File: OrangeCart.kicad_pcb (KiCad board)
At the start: 4 copper layers, 62 x 50 mm, 131 parts, among them J1 Conn_02x11_Odd_Even, J2 UART, J3 USB_B_Mini, J4 MicroSd, J6 JTAG, SW1 SW_Push, U1 FAN53541, U10 NCP115-2.5, U11 74AHCV17A, U12 74LVC3G17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

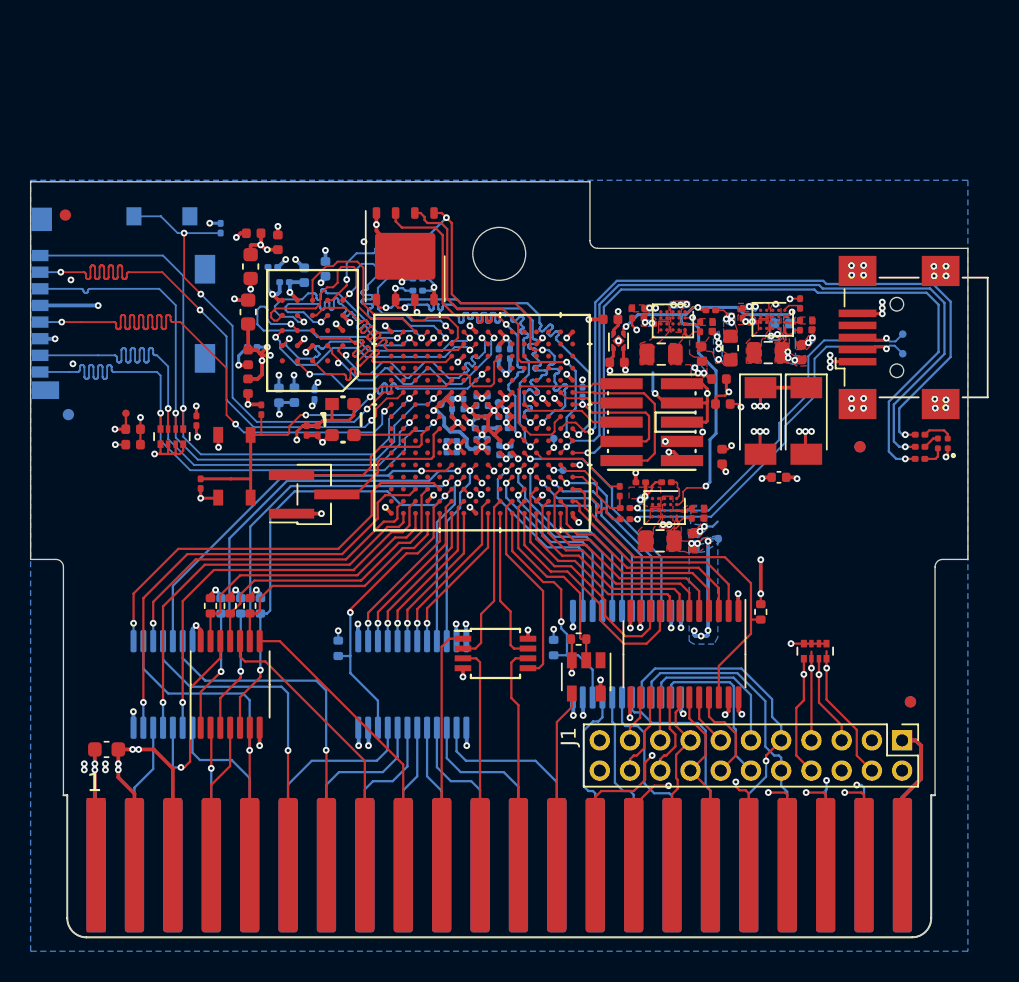
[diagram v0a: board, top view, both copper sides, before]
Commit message: Replace LED with THT version
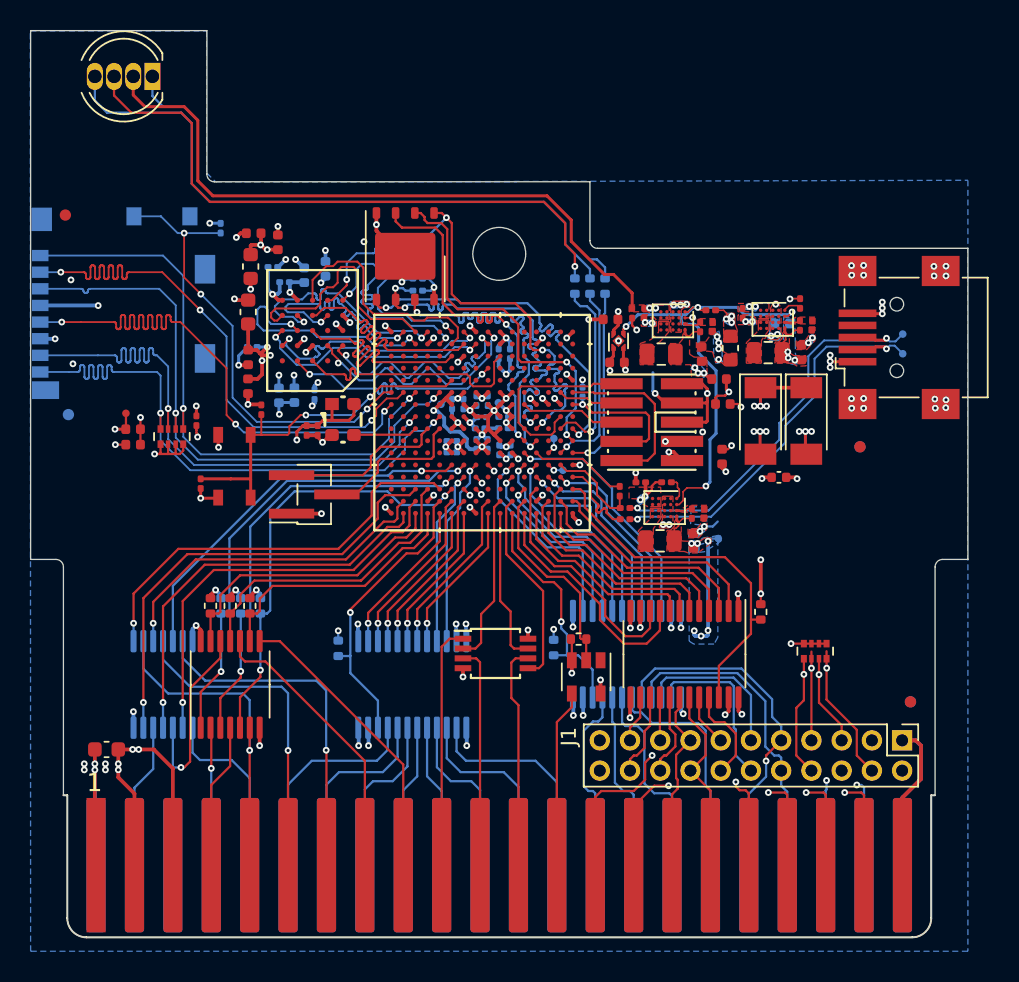
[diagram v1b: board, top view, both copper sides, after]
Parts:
- D1: value LED_ARGB -> LED_RABG; footprint gkl_led:0404LED_RGB -> LED_THT:LED_D5.0mm-4_RGB
- R22: value 1.5k -> 249; footprint Resistor_SMD:R_0201_0603Metric -> Resistor_SMD:R_0402_1005Metric; moved to B.Cu
- R23: value 4.7k -> 120; footprint Resistor_SMD:R_0201_0603Metric -> Resistor_SMD:R_0402_1005Metric; moved to B.Cu
- R24: value 3.57k -> 120; footprint Resistor_SMD:R_0201_0603Metric -> Resistor_SMD:R_0402_1005Metric; moved to B.Cu
- moved D1 57.6 mm to (57.1, 73.1), turned to 180 degrees
- moved R24 24.9 mm to (85.0, 87.0), turned to 90 degrees
- moved R23 24.3 mm to (86.0, 87.0), turned to 90 degrees
- moved R22 23.8 mm to (87.0, 87.0), turned to 90 degrees
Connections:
- D1 pad 1: P3.3V -> Net-(D1-Pad1)
- D1 pad 2: Net-(D1-Pad2) -> VSYS
- R22 pad 2: Net-(D1-Pad2) -> Net-(D1-Pad1)
- R23 pad 2: Net-(D1-Pad3) -> Net-(D1-Pad4)
- R24 pad 2: Net-(D1-Pad4) -> Net-(D1-Pad3)
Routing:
- net VSYS: track 33.9 -> 77.7 mm
- net Net-(D1-Pad4): track 2.03 -> 42.7 mm
- net Net-(D1-Pad1): track 0.00 -> 39.8 mm
- net Net-(D1-Pad3): track 1.08 -> 40.9 mm, vias 0 -> 1
- net LED_R: track 47.4 -> 12.2 mm, vias 2 -> 1
- net LED_G: track 47.7 -> 12.7 mm, vias 2 -> 1
- net LED_B: track 46.9 -> 12.5 mm, vias 2 -> 1
- net Net-(D1-Pad2): track 1.47 -> 0.00 mm
- net P3.3V: track 49.0 -> 48.4 mm, vias 26 -> 25
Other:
- board size 62 x 50 mm -> 62 x 60 mm

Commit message: Replace pushbutton with THT version
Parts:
- SW1: footprint gkl_misc:PTS_810_SMT_Switch -> TE:TPB11CGPC004
- moved FID5 23.7 mm to (50.7, 71.8)
- moved SW1 21.1 mm to (52.5, 80.3)
- moved C76 15.5 mm to (61.6, 84.6), turned to 0 degrees
- moved R4 11.7 mm to (61.6, 83.8), turned to 180 degrees
- moved FID4 10.5 mm to (50.7, 71.8)
- moved D1 0.50 mm to (57.1, 73.6)
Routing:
- net USER_BUTTON: track 23.9 -> 33.8 mm
- net GND: track 145.5 -> 143.7 mm, vias 118 -> 117
- net VSYS: track 77.7 -> 77.2 mm
- net Net-(D1-Pad4): track 42.7 -> 42.2 mm
- net Net-(D1-Pad3): track 40.9 -> 40.4 mm
- net Net-(D1-Pad1): track 39.8 -> 39.3 mm

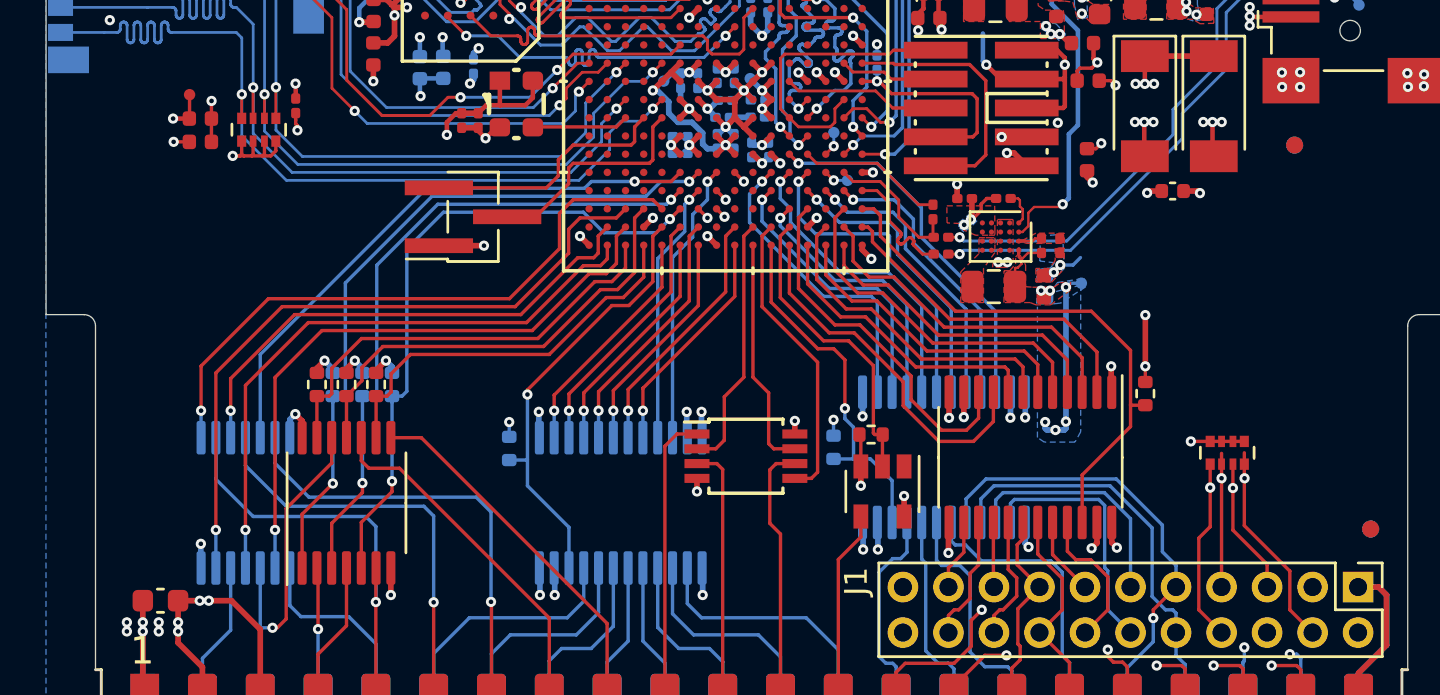
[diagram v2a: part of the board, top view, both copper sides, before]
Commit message: Moved fiducials
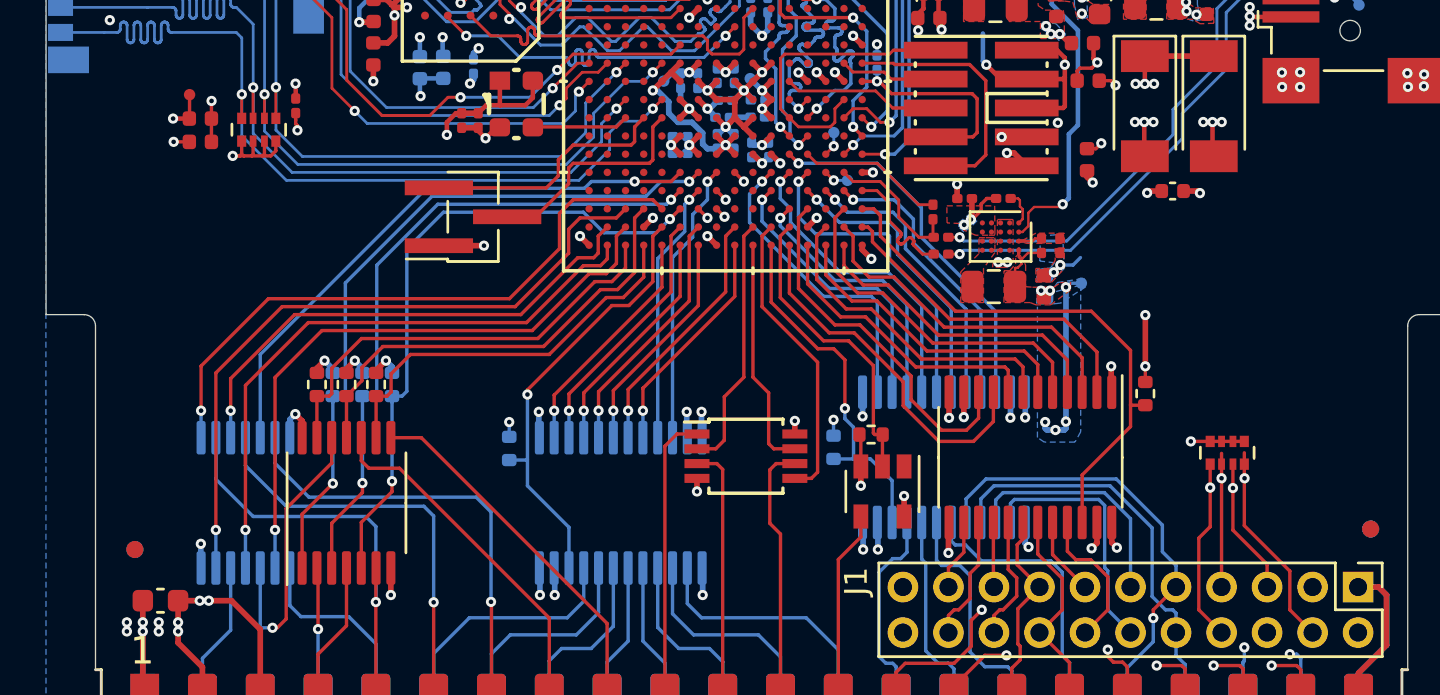
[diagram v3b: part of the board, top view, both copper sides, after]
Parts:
- moved FID3 54.0 mm to (52.9, 115.4)
- moved FID6 54.0 mm to (52.9, 115.4)

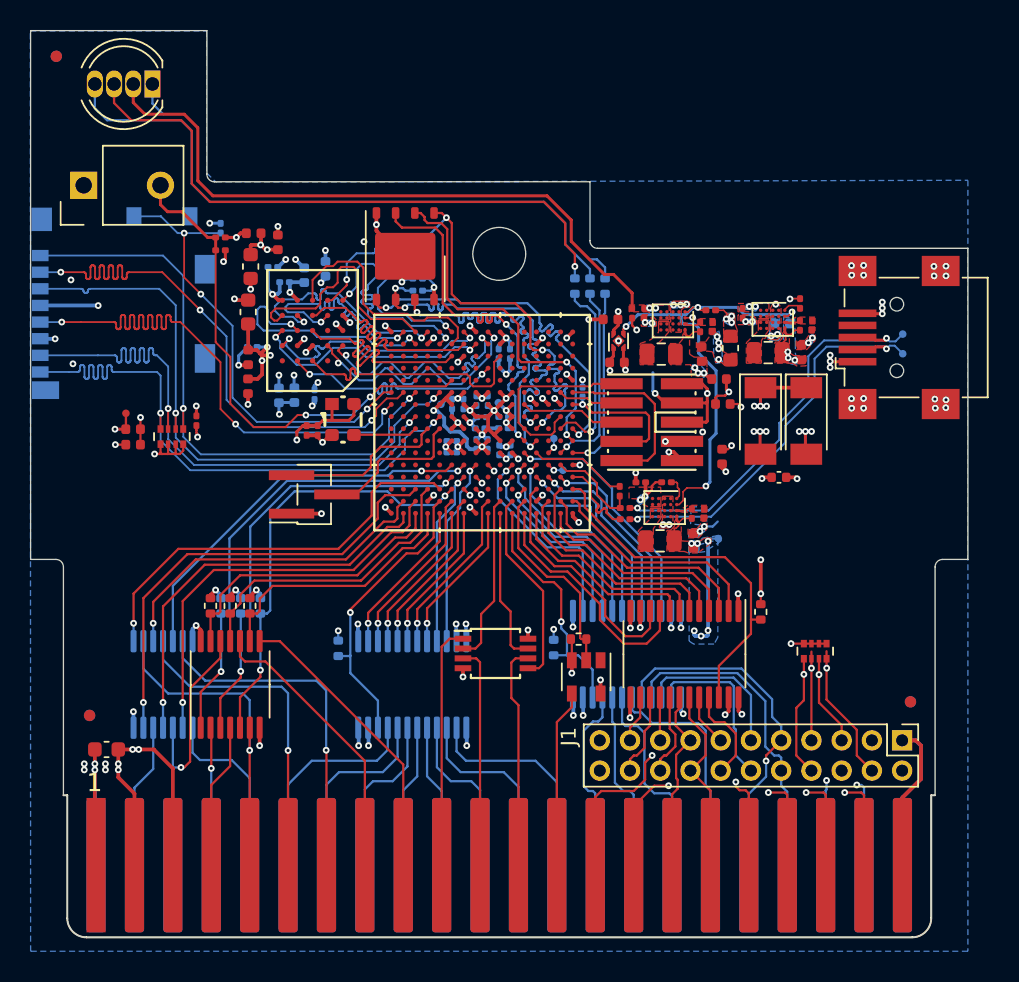
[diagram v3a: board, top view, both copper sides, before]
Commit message: Add copper pour to front layer
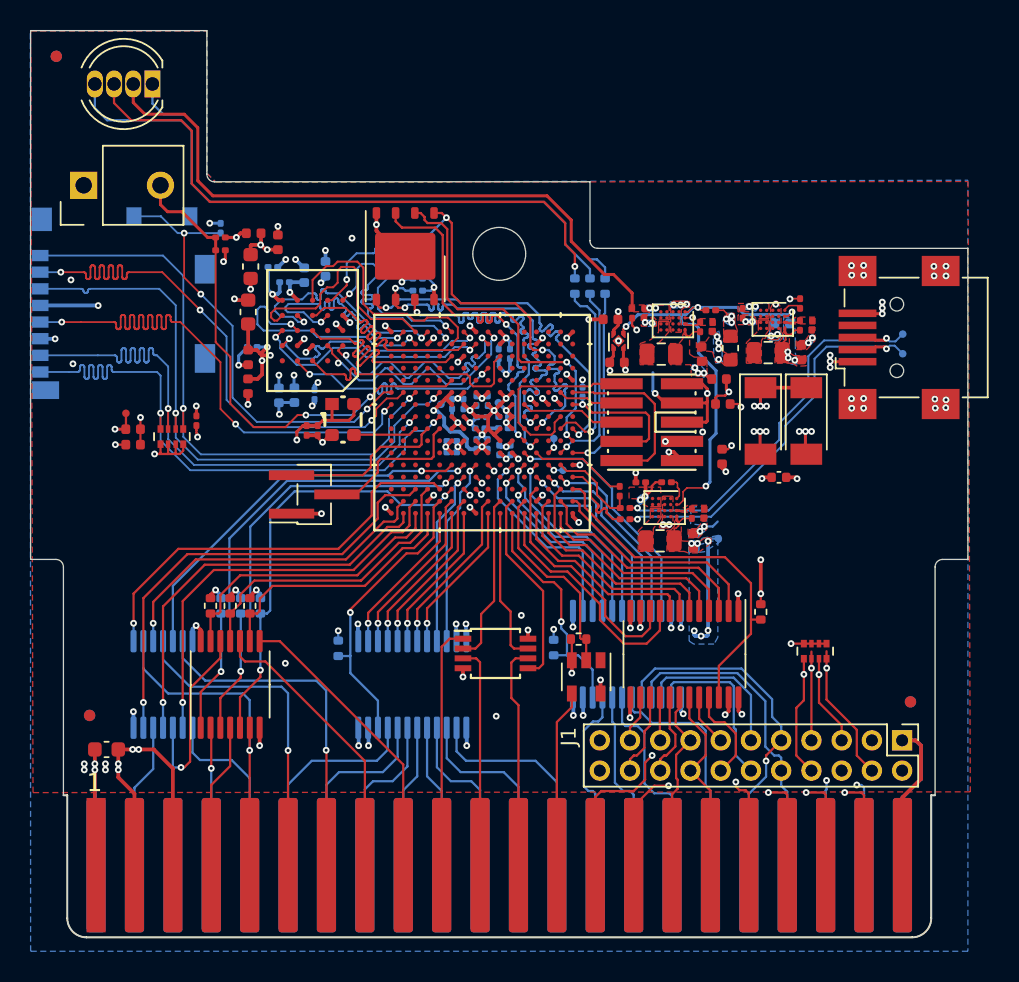
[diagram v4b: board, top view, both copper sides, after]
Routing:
- net GND: vias 117 -> 120

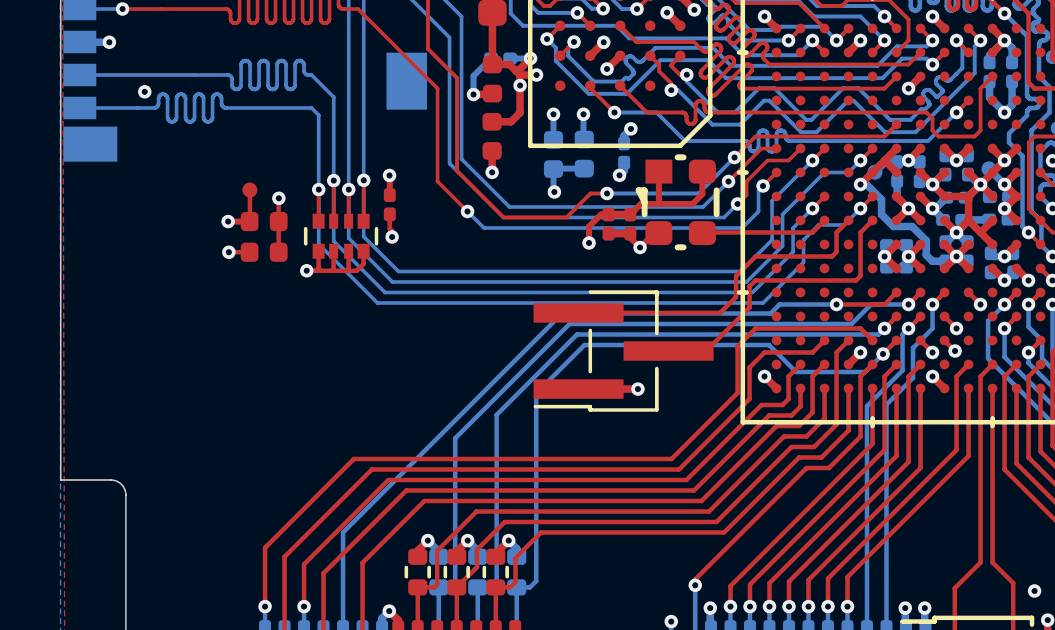
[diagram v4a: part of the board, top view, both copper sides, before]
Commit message: Move UART connector
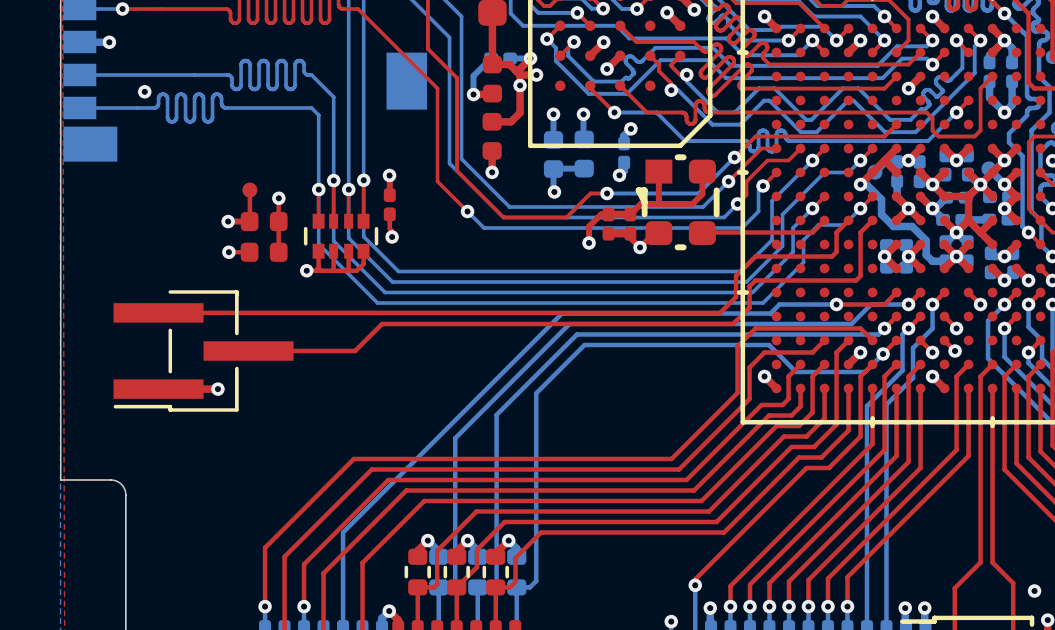
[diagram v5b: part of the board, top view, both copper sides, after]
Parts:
- moved J2 14.0 mm to (53.8, 100.8)
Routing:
- net /sheetFPGA/TXD: track 11.1 -> 25.1 mm
- net /sheetFPGA/RXD: track 9.86 -> 23.9 mm

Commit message: Adjust RGB LED resistors after measurements
Measurement over resistors in testbench gave

R: 2.52V -> 210 ohm for 12.0 mA
G: 1.5V  -> 124 ohm for 12.1 mA
B: 1.48V -> 124 ohm for 11.9 mA
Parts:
- R22: value 249 -> 210
- R23, R24: value 120 -> 124

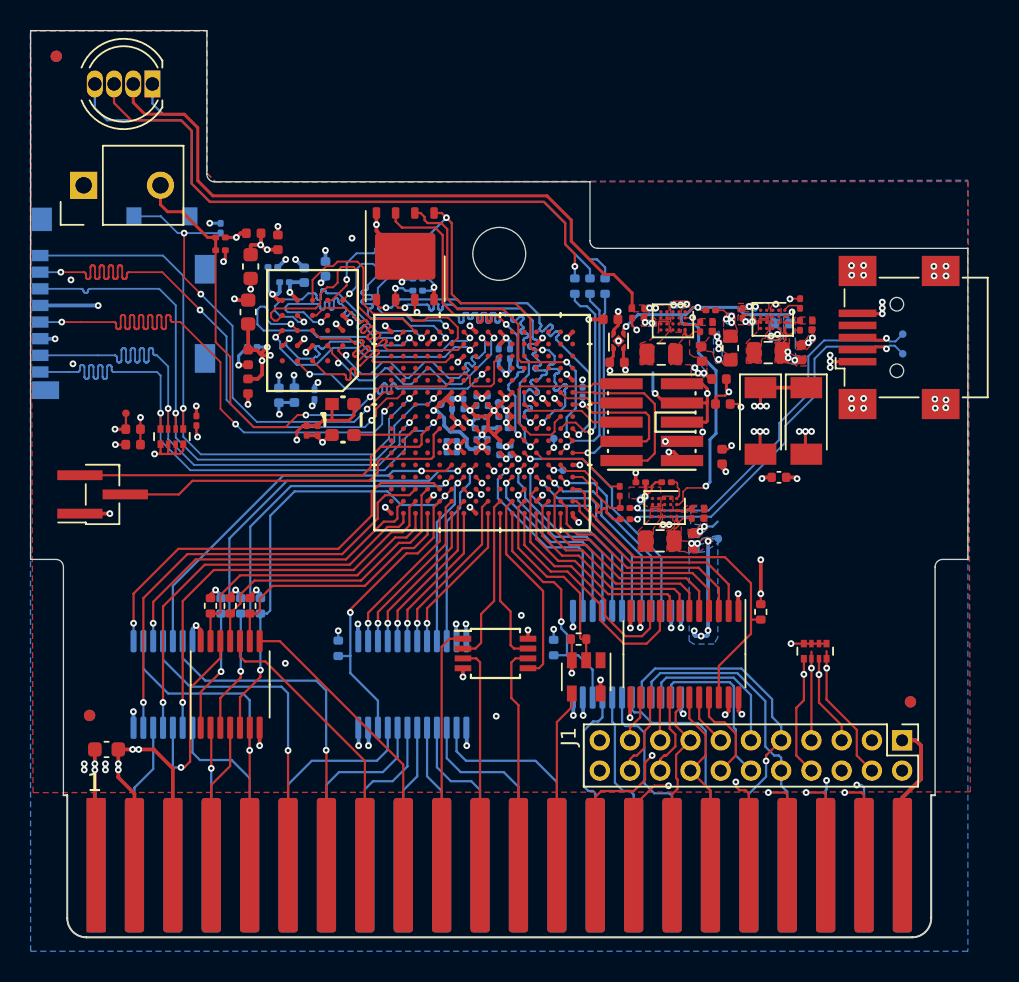
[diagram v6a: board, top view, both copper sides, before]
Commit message: Add some more margin between traces and board edge
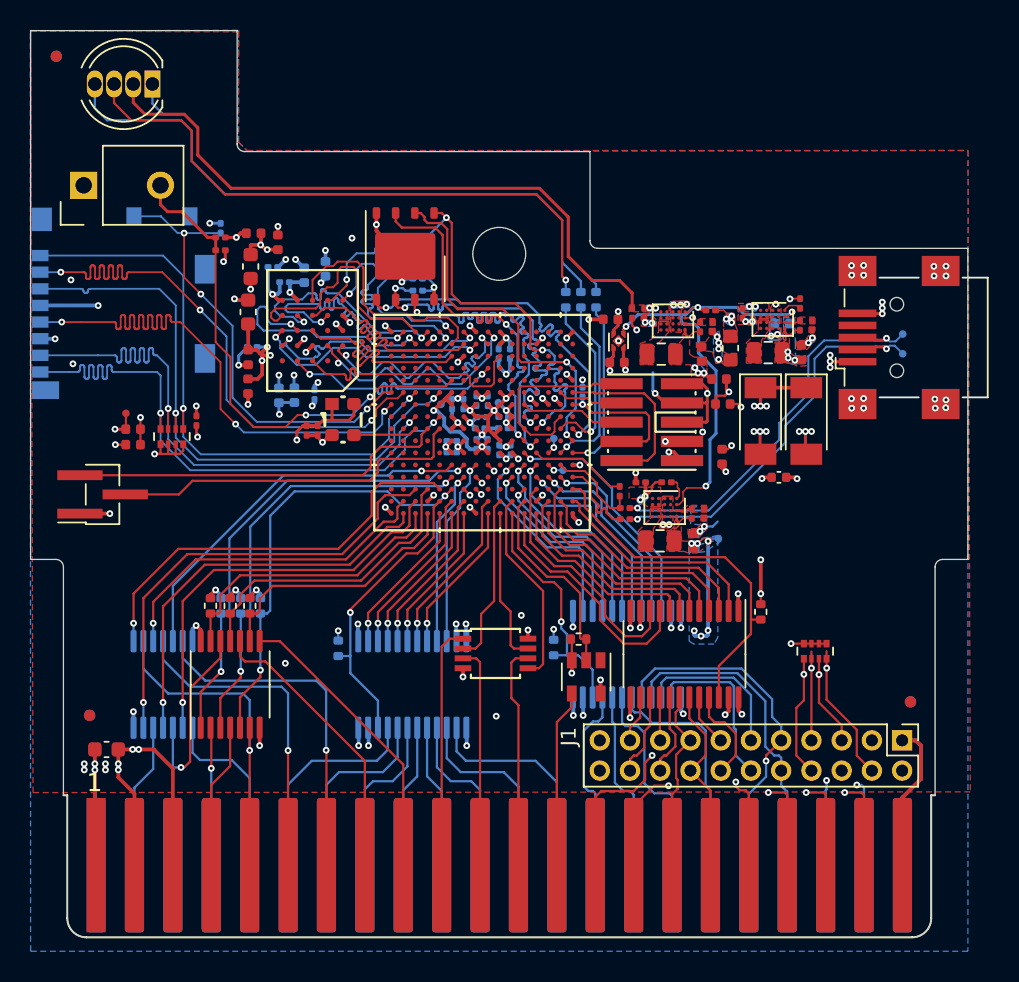
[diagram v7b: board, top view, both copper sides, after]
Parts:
- moved R22 1.08 mm to (86.4, 87.9)
- moved R23 1.08 mm to (85.4, 87.9)
- moved R24 1.08 mm to (84.4, 87.9)
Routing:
- net LED_B: track 12.5 -> 11.6 mm
- net LED_R: track 12.2 -> 11.5 mm
- net LED_G: track 12.7 -> 12.0 mm
- net Net-(D1-Pad1): track 39.3 -> 38.7 mm
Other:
- outline, holes or cut-outs redrawn
